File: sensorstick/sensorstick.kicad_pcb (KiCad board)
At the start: 2 copper layers, 85 x 23 mm, 5 parts, among them U1 ESP32-C3_SUPERMINI

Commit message: progress
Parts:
- removed BT1: Battery_Cell, CustomLibrary:BatteryHolder_Keystone_1060_1x2032
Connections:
- OLED1 pad 3: unconnected-(OLED1-SCL-Pad3) -> i2c_scl
- OLED1 pad 4: unconnected-(OLED1-SDA-Pad4) -> i2c_sda
- U1 pad 0: unconnected-(U1-GPIO0-Pad0) -> i2c_scl
- U1 pad 1: unconnected-(U1-GPIO1-Pad1) -> i2c_sda
- U2 pad 3: unconnected-(U2-SCL-Pad3) -> i2c_scl
- U2 pad 4: unconnected-(U2-SDA-Pad4) -> i2c_sda
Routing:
- net i2c_sda: track 0.00 -> 66.6 mm, vias 0 -> 1
- net i2c_scl: track 0.00 -> 63.0 mm, vias 0 -> 1
- net +3.3V: track 65.6 -> 58.6 mm, vias 0 -> 1
- net +5V: track 25.5 -> 30.0 mm, vias 0 -> 2
- net GND: vias 0 -> 1

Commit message: add condensator
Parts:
- added C1: C, Capacitor_SMD:C_0603_1608Metric, F.Cu at (127.3, 108.9)
- added C2: C, Capacitor_SMD:C_0603_1608Metric, F.Cu at (93.5, 101.6)
- added C3: C, Capacitor_SMD:C_0603_1608Metric, F.Cu at (88.2, 90.7)
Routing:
- net +3.3V: track 58.6 -> 69.8 mm
- net +5V: track 30.0 -> 33.1 mm

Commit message: update
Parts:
- moved C2 4.11 mm to (89.4, 101.9)
- moved C1 1.33 mm to (128.4, 108.2)
- moved OLED1 1.13 mm to (91.9, 99.2)
- moved U2 1.00 mm to (133.1, 107.8)
- moved U1 0.10 mm to (77.4, 99.0)
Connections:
- USB1 pad 5: unconnected-(USB1-Pad5) -> GND
- USB1 pad 6: unconnected-(USB1-Pad6) -> GND
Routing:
- net +3.3V: track 69.8 -> 0.00 mm, vias 1 -> 0
- net i2c_sda: track 66.6 -> 0.00 mm, vias 1 -> 0
- net i2c_scl: track 63.0 -> 0.00 mm, vias 1 -> 0
- net +5V: track 33.1 -> 0.00 mm, vias 2 -> 0
- net GND: vias 1 -> 0
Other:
- board text added: "${TITLE} by ${COMPANY} (rev. ${REVISION}) ${COMMENT1}"

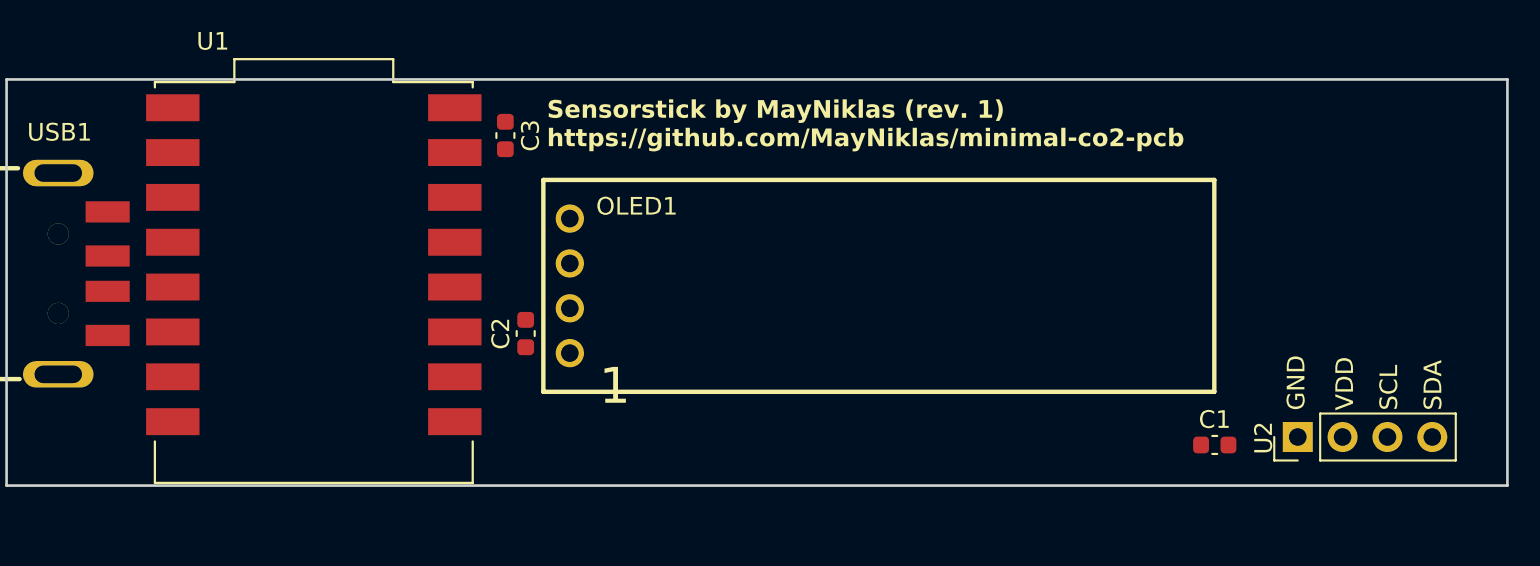
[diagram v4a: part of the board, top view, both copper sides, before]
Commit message: updating routing
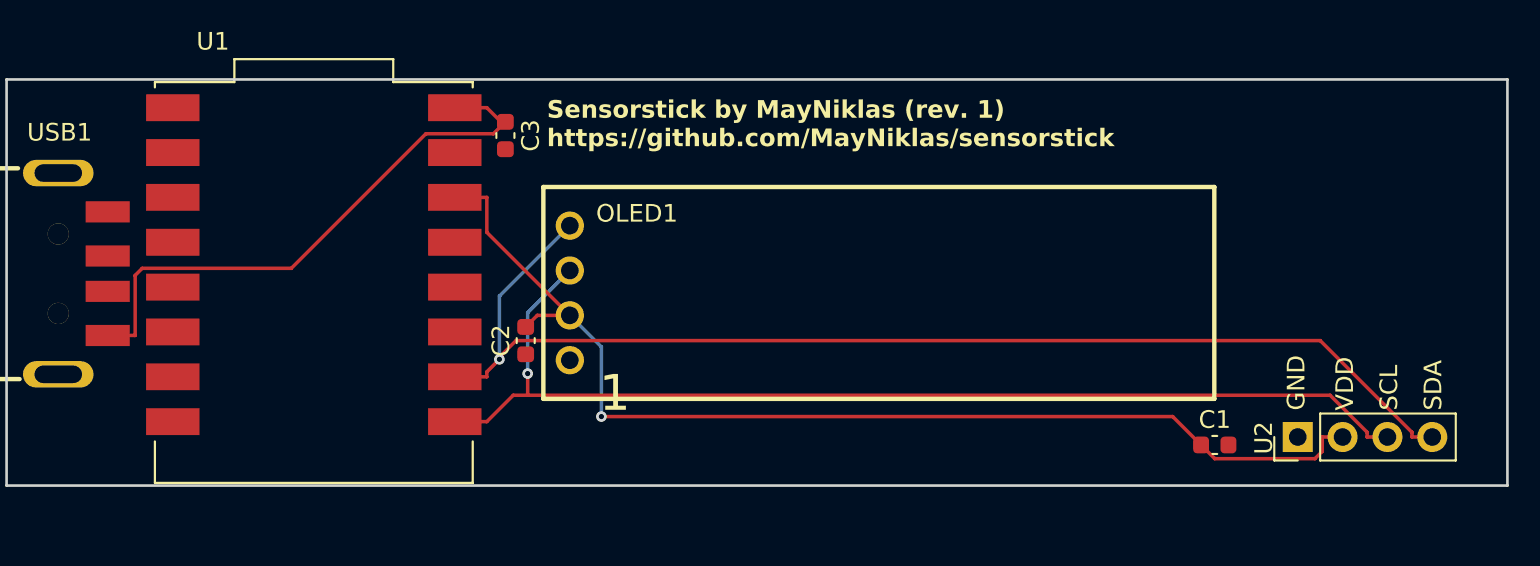
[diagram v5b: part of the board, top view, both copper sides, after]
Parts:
- moved C2 0.40 mm to (89.4, 102.3)
- moved OLED1 0.40 mm to (91.9, 99.6)
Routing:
- net i2c_sda: track 0.00 -> 68.1 mm, vias 0 -> 1
- net +3.3V: track 0.00 -> 63.6 mm, vias 0 -> 1
- net i2c_scl: track 0.00 -> 62.6 mm, vias 0 -> 1
- net +5V: track 0.00 -> 32.7 mm
